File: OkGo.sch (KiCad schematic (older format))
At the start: 27 parts

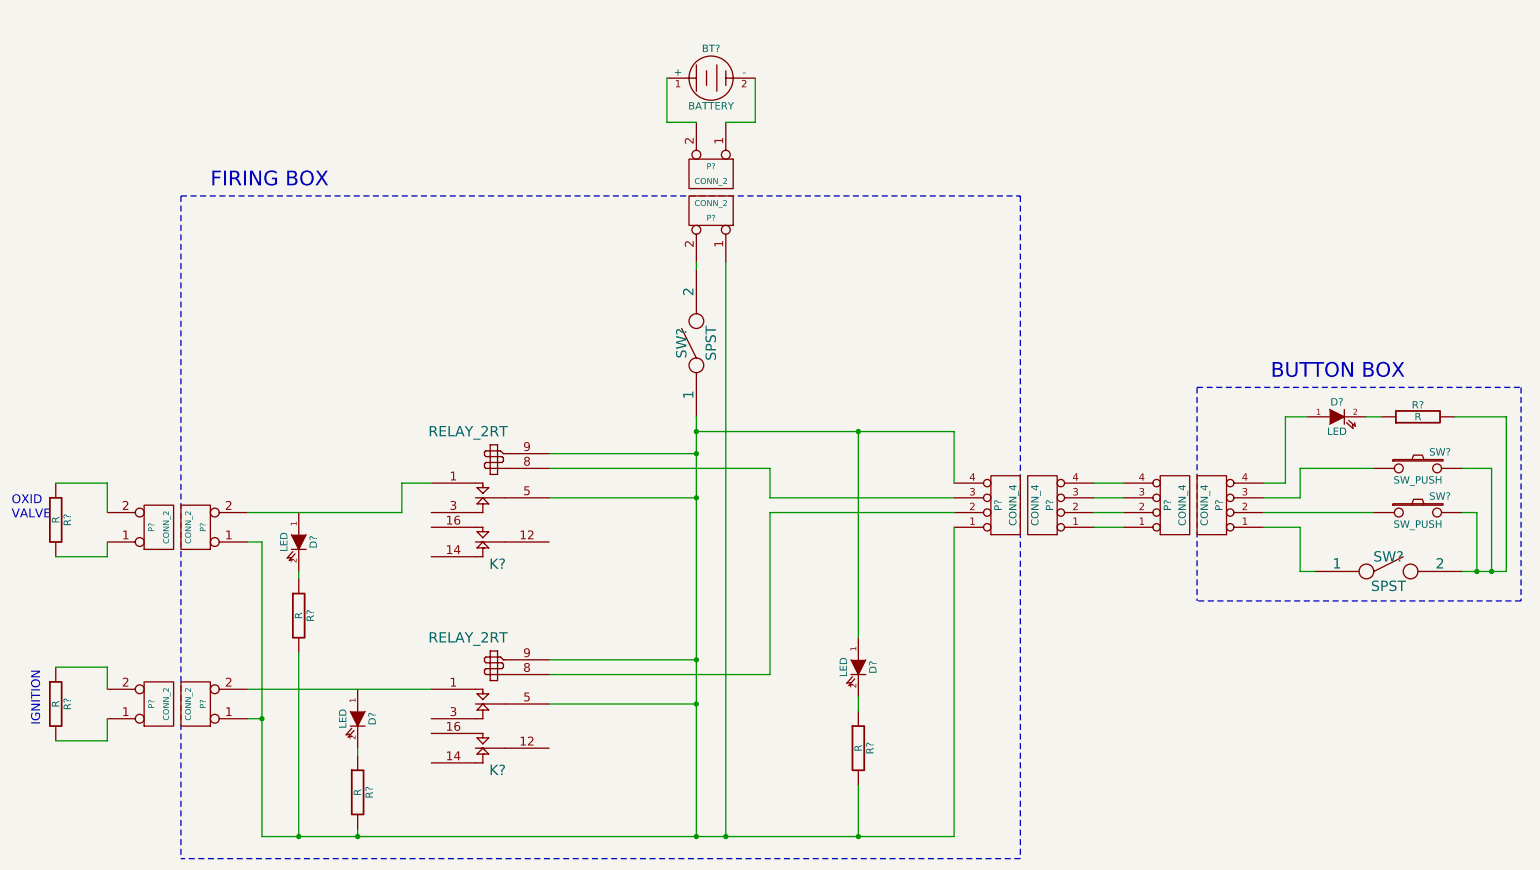
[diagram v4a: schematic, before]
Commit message: Added handy schematic labels
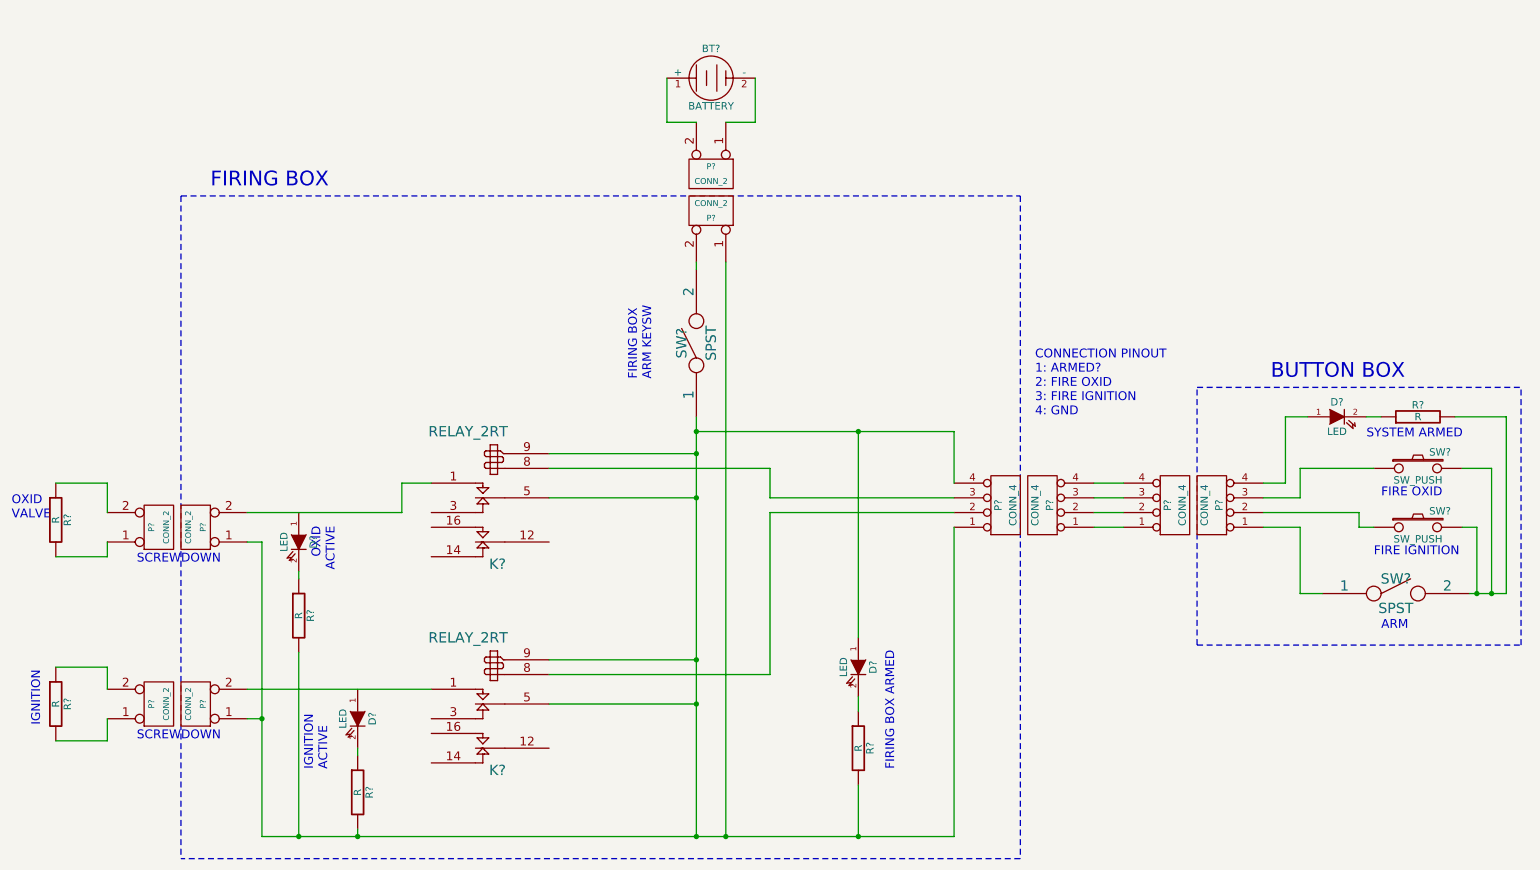
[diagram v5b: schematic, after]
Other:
- note added: "ARM"
- note added: "CONNECTION PINOUT\n1: ARMED?\n2: FIRE OXID\n3: FIRE IGNITION\n4: GND"
- note added: "FIRE IGNITION"
- note added: "FIRE OXID"
- note added: "FIRING BOX ARMED"
- note added: "FIRING BOX\nARM KEYSW"
- note added: "IGNITION\nACTIVE"
- note added: "OXID\nACTIVE"
- note added: "SCREWDOWN"
- note added: "SYSTEM ARMED"
- moved on the sheet: SW?
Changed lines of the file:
@@
-EESchema Schematic File Version 2  date 25/11/2012 14:01:06
+EESchema Schematic File Version 2  date 25/11/2012 14:20:29
 LIBS:power
 LIBS:device
@@
 Comment4 ""
 $EndDescr
+Text Notes 6550 5550 1    60   ~ 0
+FIRING BOX ARMED
+Text Notes 7500 3150 0    60   ~ 0
+CONNECTION PINOUT\n1: ARMED?\n2: FIRE OXID\n3: FIRE IGNITION\n4: GND
+Wire Notes Line
+	10800 4700 10800 2950
+Wire Notes Line
+	8600 4700 10800 4700
+Wire Notes Line
+	8600 4700 8600 2950
+Wire Wire Line
+	10500 4350 10500 3900
+Wire Wire Line
+	10700 3150 10700 4350
+Wire Wire Line
+	9300 3900 9300 4350
 Connection ~ 6300 6000
 Wire Wire Line
@@
 Wire Wire Line
 	7900 3600 8100 3600
-Connection ~ 10600 4200
-Wire Wire Line
-	10400 4200 10700 4200
-Wire Wire Line
-	10700 4200 10700 3150
 Wire Wire Line
 	10700 3150 10350 3150
@@
 Wire Wire Line
 	1200 3600 850  3600
-Connection ~ 10500 4200
-Wire Wire Line
-	10600 4200 10600 3500
-Wire Wire Line
-	10600 3500 10400 3500
-Wire Wire Line
-	9400 4200 9300 4200
-Wire Wire Line
-	9300 4200 9300 3900
+Wire Wire Line
+	10400 3500 10600 3500
 Wire Wire Line
 	9300 3900 9050 3900
@@
 	9300 3500 9800 3500
 Wire Wire Line
-	9050 3800 9800 3800
-Wire Wire Line
-	10400 3800 10500 3800
-Wire Wire Line
-	10500 3800 10500 4200
+	10500 3900 10400 3900
 Wire Wire Line
 	850  4100 1200 4100
@@
 	9750 3150 9850 3150
 Wire Notes Line
-	8600 2950 8600 4400
-Wire Notes Line
 	8600 2950 10800 2950
-Wire Notes Line
-	10800 2950 10800 4400
-Wire Notes Line
-	10800 4400 8600 4400
 Wire Wire Line
 	8100 3700 7900 3700
@@
 Wire Wire Line
 	6300 5050 6300 5150
+Wire Wire Line
+	9050 3800 9700 3800
+Wire Wire Line
+	9700 3800 9700 3900
+Wire Wire Line
+	9700 3900 9800 3900
+Wire Wire Line
+	10600 3500 10600 4350
+Wire Wire Line
+	9300 4350 9450 4350
+Wire Wire Line
+	10700 4350 10450 4350
+Connection ~ 10600 4350
+Connection ~ 10500 4350
+Text Notes 9850 4600 0    60   ~ 0
+ARM
+Text Notes 9800 4100 0    60   ~ 0
+FIRE IGNITION
+Text Notes 9850 3700 0    60   ~ 0
+FIRE OXID
+Text Notes 9750 3300 0    60   ~ 0
+SYSTEM ARMED
+Text Notes 4900 2900 1    60   ~ 0
+FIRING BOX\nARM KEYSW
+Text Notes 2700 5550 1    60   ~ 0
+IGNITION\nACTIVE
+Text Notes 2750 3900 3    60   ~ 0
+OXID\nACTIVE
+Text Notes 1400 4150 0    60   ~ 0
+SCREWDOWN
+Text Notes 1400 5350 0    60   ~ 0
+SCREWDOWN
 $Comp
 L LED D?
@@
 L SPST SW?
 U 1 1 50B21E62
-P 9900 4200
-F 0 "SW?" H 9900 4300 70  0000 C CNN
-F 1 "SPST" H 9900 4100 70  0000 C CNN
-	1    9900 4200
+P 9950 4350
+F 0 "SW?" H 9950 4450 70  0000 C CNN
+F 1 "SPST" H 9950 4250 70  0000 C CNN
+	1    9950 4350
 	1    0    0    -1
 $EndComp
@@
 L SW_PUSH SW?
 U 1 1 50B21E58
-P 10100 3800
-F 0 "SW?" H 10250 3910 50  0000 C CNN
-F 1 "SW_PUSH" H 10100 3720 50  0000 C CNN
-	1    10100 3800
-	1    0    0    -1
-$EndComp
+P 10100 3900
+F 0 "SW?" H 10250 4010 50  0000 C CNN
+F 1 "SW_PUSH" H 10100 3820 50  0000 C CNN
+	1    10100 3900
+	1    0    0    -1
+$EndComp

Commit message: Added a few farnell parts
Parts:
- SW? (x2): Farnell (none) -> SW03394
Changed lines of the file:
@@
-EESchema Schematic File Version 2  date 25/11/2012 14:20:29
+EESchema Schematic File Version 2  date 25/11/2012 18:38:46
 LIBS:power
 LIBS:device
@@
 F 0 "SW?" H 10250 4010 50  0000 C CNN
 F 1 "SW_PUSH" H 10100 3820 50  0000 C CNN
+F 4 "SW03394" H 10100 3900 60  0001 C CNN "Farnell"
 	1    10100 3900
 	1    0    0    -1
@@
 F 0 "SW?" H 10250 3610 50  0000 C CNN
 F 1 "SW_PUSH" H 10100 3420 50  0000 C CNN
+F 4 "SW03394" H 10100 3500 60  0001 C CNN "Farnell"
 	1    10100 3500
 	1    0    0    -1

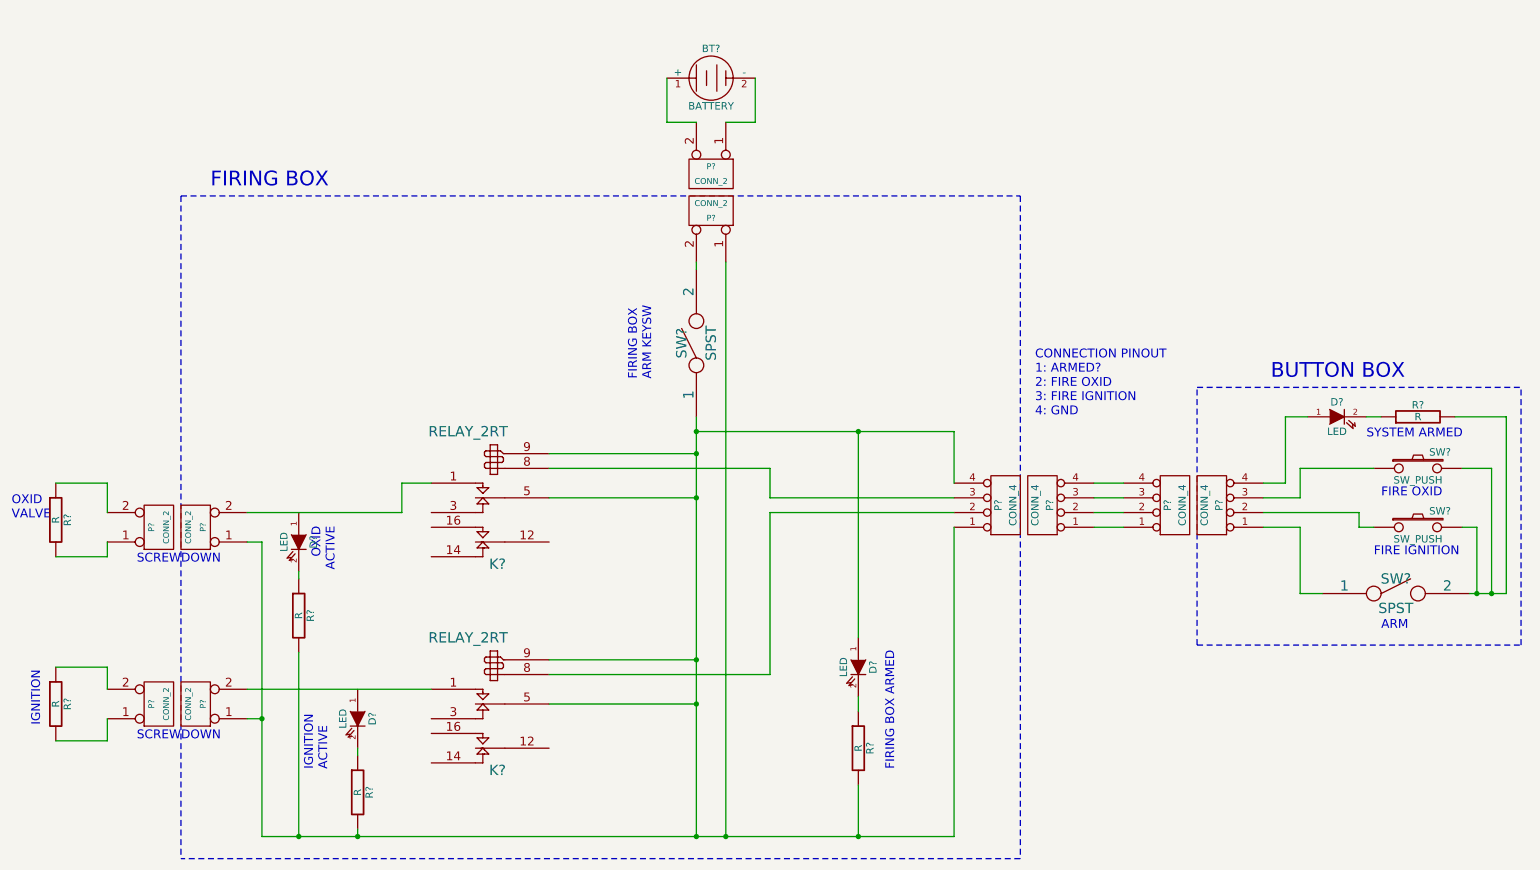
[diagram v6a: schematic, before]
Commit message: Updated schematic to reflect ordered parts
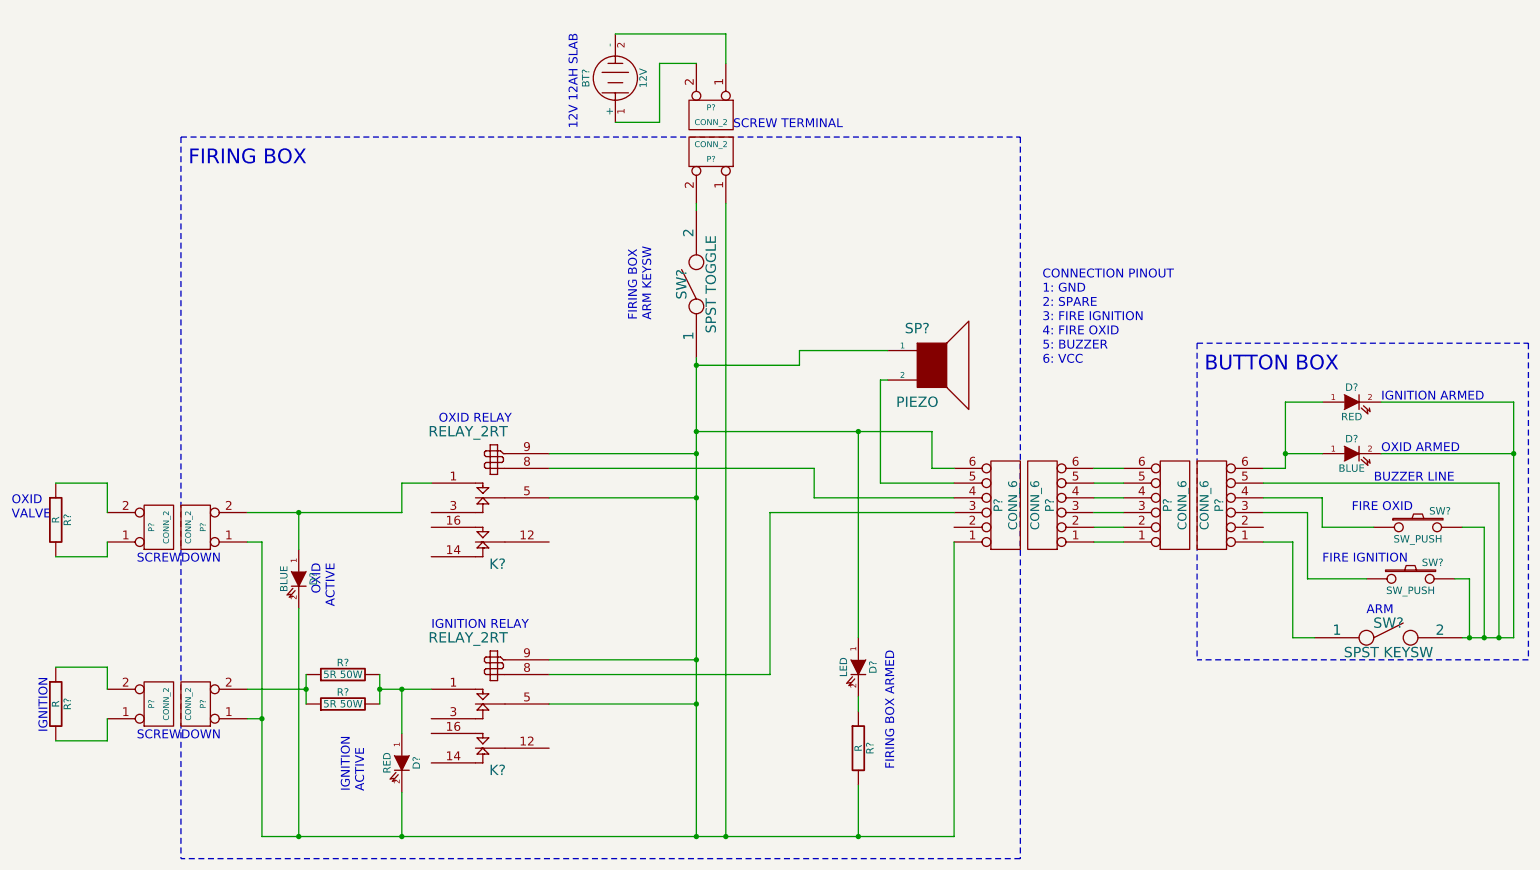
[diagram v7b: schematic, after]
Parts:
- removed P? (x4): CONN_4, symbol CONN_4
- removed R? (x3): R, symbol R
- added D?: RED, symbol LED
- added P? (x4): CONN_6, symbol CONN_6
- added R? (x2): 5R 50W, symbol R
- added SP?: PIEZO, symbol SPEAKER
- BT?: value BATTERY -> 12V
- D? (x2): value LED -> BLUE
- D?: value LED -> RED
- SW?: value SPST -> SPST TOGGLE
- SW?: value SPST -> SPST KEYSW
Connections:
- net at D?.1 (A), K?.5 (C1), K?.5 (C1)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: now also D?.2 (K), D?.2 (K), P?.1, P?.6, SP?.1
- net at K?.1 (T1), P?.2 (PM): now also D?.1 (A)
- net at K?.8: now also P?.4
- net at K?.1 (T1): now also D?.1 (A), R?.2, R?.2; no longer P?.2 (PM)
- net at K?.8: now also P?.3
- net at SW?.1: now also P?.3
- net at SW?.2, SW?.2, SW?.2: now also D?.2 (K), D?.2 (K), P?.5
- net at SW?.1: now also P?.4
- net at SW?.1: now also P?.1
- net at D?.1 (A): now also D?.1 (A), P?.6
- new net: P?.2 (PM), R?.1, R?.1
- new net: P?.5, SP?.2
- new net: P?.1, P?.1
- new net: P?.2, P?.2
- new net: P?.3, P?.3
- new net: P?.4, P?.4
- new net: P?.5, P?.5
- new net: P?.6, P?.6
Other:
- note added: "12V 12AH SLAB"
- note added: "BUZZER LINE"
- note added: "CONNECTION PINOUT\n1: GND\n2: SPARE\n3: FIRE IGNITION\n4: FIRE OXID\n5: BUZZER\n6: VCC"
- note added: "IGNITION ARMED"
- note added: "IGNITION RELAY"
- note added: "OXID ARMED"
- note added: "OXID RELAY"
- note added: "SCREW TERMINAL"
- note removed: "CONNECTION PINOUT\n1: ARMED?\n2: FIRE OXID\n3: FIRE IGNITION\n4: GND"
- note removed: "SYSTEM ARMED"
- moved on the sheet: BT?, D?, P?, SW?

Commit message: Made schematic a little prettier
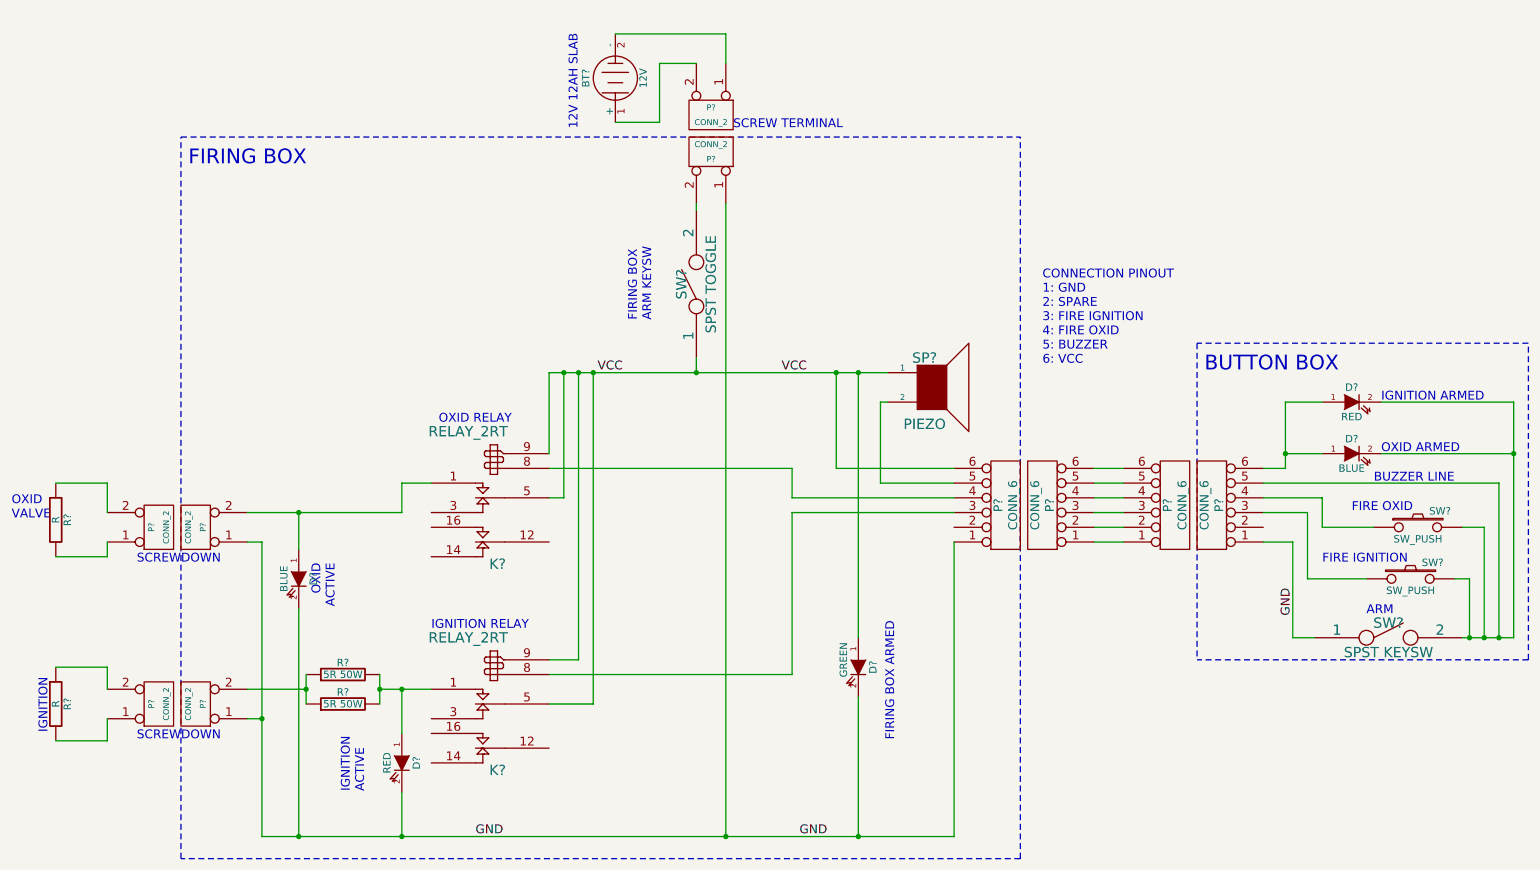
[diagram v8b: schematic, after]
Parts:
- removed R?: R, symbol R
- D?: value LED -> GREEN
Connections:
- net VCC: now reaches D?.1 (A), K?.5 (C1), K?.5 (C1), K?.9, K?.9, P?.6, SP?.1, SW?.1
- net VCC: no longer D?.2 (K), D?.2 (K), P?.1, P?.1 (P1), P?.1 (P1), P?.1 (P1)
- net GND: now reaches P?.1, SW?.1
- net GND: now also D?.2 (K), D?.2 (K), D?.2 (K), P?.1, P?.1 (P1), P?.1 (P1), P?.1 (P1)
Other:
- moved on the sheet: SP?
